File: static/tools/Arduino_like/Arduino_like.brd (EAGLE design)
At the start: 63.5 x 41.6 mm, 19 parts, among them IC1 MEGA8-P

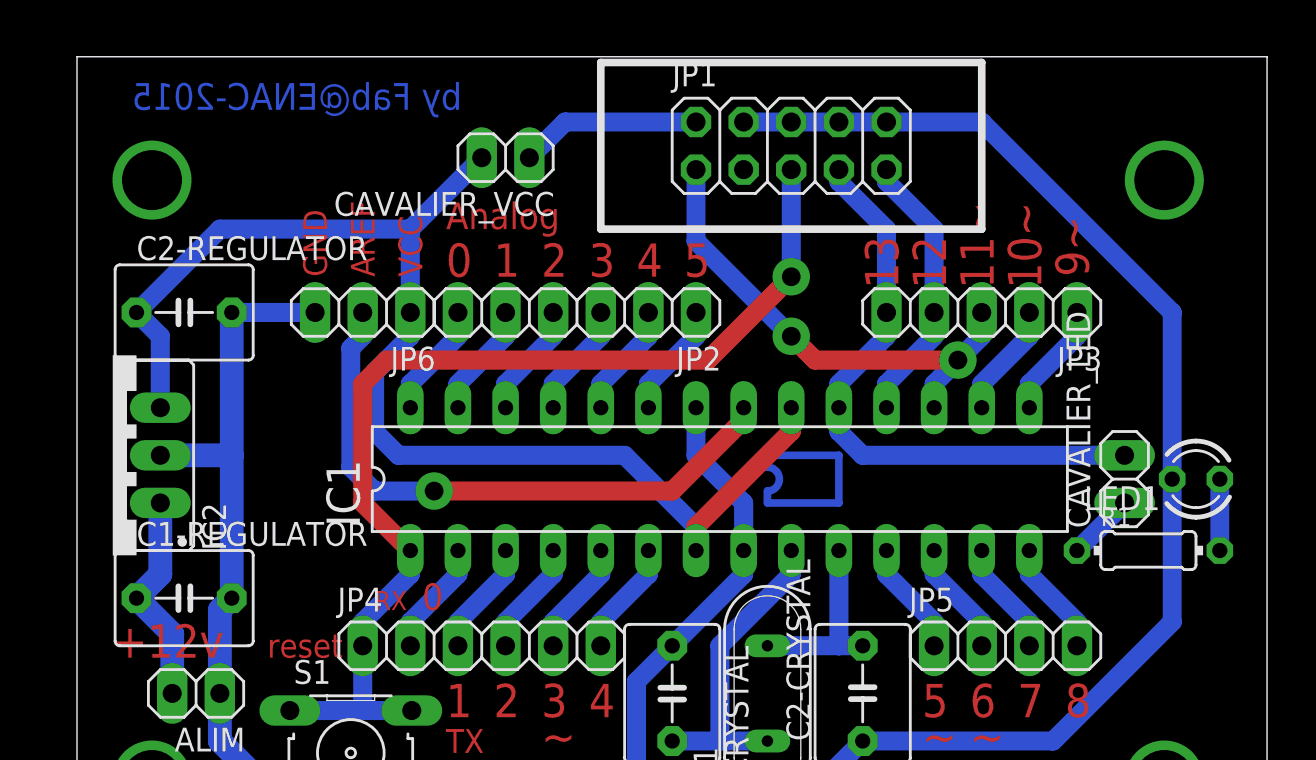
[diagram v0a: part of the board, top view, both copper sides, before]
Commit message: [Arduino_like] change some dimensions.
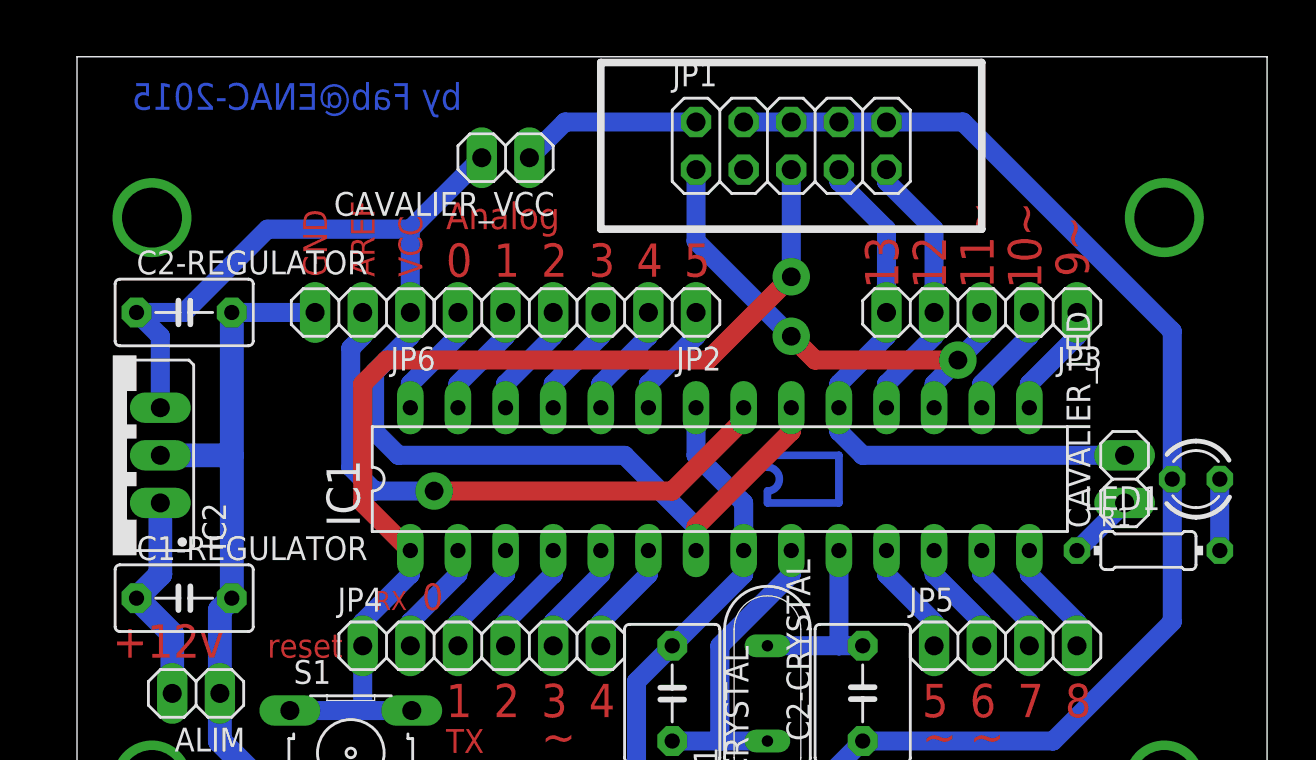
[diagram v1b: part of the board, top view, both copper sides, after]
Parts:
- C1-REGULATOR, C2-REGULATOR: device capacitor-wima:C5B5 -> capacitor-wima:C5B3.5
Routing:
- net GND: track 154.1 -> 153.6 mm
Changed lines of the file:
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@@
 <setting verticaltext="up"/>
 </settings>
-<grid distance="0.1" unitdist="inch" unit="inch" style="lines" multiple="1" display="yes" altdistance="0.025" altunitdist="inch" altunit="inch"/>
+<grid distance="1" unitdist="mm" unit="mm" style="lines" multiple="1" display="yes" altdistance="0.025" altunitdist="inch" altunit="inch"/>
 <layers>
 <layer number="1" name="Top" color="4" fill="1" visible="yes" active="yes"/>
@@
 <text x="10.16" y="9.525" size="1.27" layer="1">reset</text>
 <dimension x1="4" y1="3" x2="58" y2="3" x3="31" y3="-25.4" layer="47"/>
-<dimension x1="58" y1="3" x2="58" y2="35" x3="84.359996875" y3="19" layer="47"/>
-<dimension x1="4" y1="3" x2="4" y2="35" x3="-5" y3="19" layer="47"/>
+<dimension x1="58" y1="3" x2="58" y2="33" x3="84.359996875" y3="18" layer="47"/>
+<dimension x1="4" y1="3" x2="4" y2="33" x3="-5" y3="18" layer="47"/>
 </plain>
 <attributes>
@@
 <element name="C2-CRYSTAL" library="capacitor-wima" package="C5B5" value="20 pF" x="41.91" y="7.62" rot="R90"/>
 <element name="IC2" library="v-reg" package="78XXS" value="" x="1.905" y="20.32" rot="R90"/>
-<element name="C1-REGULATOR" library="capacitor-wima" package="C5B5" value="" x="5.715" y="12.7"/>
-<element name="C2-REGULATOR" library="capacitor-wima" package="C5B5" value="" x="5.715" y="27.94"/>
+<element name="C1-REGULATOR" library="capacitor-wima" package="C5B3.5" value="" x="5.715" y="12.7"/>
+<element name="C2-REGULATOR" library="capacitor-wima" package="C5B3.5" value="" x="5.715" y="27.94"/>
 <element name="ALIM" library="pinhead" package="1X02" value="" x="6.35" y="7.62" rot="R180"/>
 <element name="JP1" library="pinhead" package="2X05" value="" x="38.1" y="36.83"/>
@@
 <wire x1="21.59" y1="36.195" x2="17.78" y2="32.385" width="1.016" layer="16"/>
 <wire x1="17.78" y1="32.385" x2="17.78" y2="27.94" width="1.016" layer="16"/>
-<wire x1="3.175" y1="27.94" x2="7.62" y2="32.385" width="1.016" layer="16"/>
-<wire x1="7.62" y1="32.385" x2="17.78" y2="32.385" width="1.016" layer="16"/>
+<wire x1="3.175" y1="27.94" x2="5.715" y2="27.94" width="1.016" layer="16"/>
+<wire x1="5.715" y1="27.94" x2="10.16" y2="32.385" width="1.016" layer="16"/>
+<wire x1="10.16" y1="32.385" x2="17.78" y2="32.385" width="1.016" layer="16"/>
 <wire x1="4.445" y1="22.86" x2="4.445" y2="26.67" width="1.016" layer="16"/>
 <wire x1="4.445" y1="26.67" x2="3.175" y2="27.94" width="1.016" layer="16"/>
@@
 <wire x1="38.1" y1="38.1" x2="40.64" y2="38.1" width="1.016" layer="16"/>
 <wire x1="40.64" y1="38.1" x2="43.18" y2="38.1" width="1.016" layer="16"/>
-<wire x1="58.42" y1="27.94" x2="48.26" y2="38.1" width="1.016" layer="16"/>
-<wire x1="48.26" y1="38.1" x2="43.18" y2="38.1" width="1.016" layer="16"/>
+<wire x1="58.42" y1="26.94" x2="47.26" y2="38.1" width="1.016" layer="16"/>
+<wire x1="47.26" y1="38.1" x2="43.18" y2="38.1" width="1.016" layer="16"/>
 <contactref element="S1" pad="4"/>
 <wire x1="8.255" y1="27.94" x2="8.255" y2="20.32" width="1.27" layer="16"/>
@@
 <wire x1="58.42" y1="11.43" x2="52.07" y2="5.08" width="1.016" layer="16"/>
 <wire x1="52.07" y1="5.08" x2="41.91" y2="5.08" width="1.016" layer="16"/>
-<wire x1="58.42" y1="19.05" x2="58.42" y2="27.94" width="1.016" layer="16"/>
+<wire x1="58.42" y1="19.05" x2="58.42" y2="26.94" width="1.016" layer="16"/>
 <wire x1="11.3538" y1="2.1844" x2="10.0838" y2="2.6162" width="1.27" layer="16"/>
 <wire x1="10.0838" y1="2.6162" x2="7.62" y2="5.08" width="1.27" layer="16"/>
@@
 </signal>
 <signal name="N$43">
-<via x="58" y="35" extent="1-16" drill="3.2"/>
+<via x="58" y="33" extent="1-16" drill="3.2"/>
 </signal>
 <signal name="N$44">
-<via x="4" y="35" extent="1-16" drill="3.2"/>
+<via x="4" y="33" extent="1-16" drill="3.2"/>
 </signal>
 </signals>
